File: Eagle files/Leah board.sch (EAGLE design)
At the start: 2 parts

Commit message: Board Tweaks
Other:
- note removed: "Adafruit Pro Trinket 5V"
- note removed: "CC 2.5 BY-SA"
- note removed: "http://adafruit.com/products/2000"
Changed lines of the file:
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@@
 <sheet>
 <plain>
-<text x="175.26" y="30.48" size="2.54" layer="94">Adafruit Pro Trinket 5V</text>
-<text x="175.26" y="25.4" size="2.54" layer="94">http://adafruit.com/products/2000</text>
-<text x="248.92" y="30.48" size="2.54" layer="94">CC 2.5 BY-SA</text>
 </plain>
 <instances>

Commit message: Board work
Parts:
- added CONT_LED, INT_LED, LASER, POWER, PWR_LED: (no value), adafruit:JST_2PIN-SMT-RA
- added POT: (no value), adafruit:JST_3PIN
- added X_SERVO, Y_SERVO: (no value), adafruit:PINHD-1X3
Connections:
- removed net VBAT: JP1.1
- new net VCC: JP1.1, POWER.2
- net A2: now also POT.2
- net GND: now also LASER.1, POWER.1

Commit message: Modification for present.
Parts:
- added CONT_MOS, INT_MOS, LASER_MOS, PWR_MOS, X_MOS, Y_MOS: 200mA/50V, SparkFun-DiscreteSemi:MOSFET-NCHANNELBSS138
- added R1, R2, R3, R4, R5, R6: 10K, SparkFun-Resistors:10KOHM-1/10W-1%(0603)0603
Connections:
- new net CONT_PWR: CONT_LED.2, CONT_MOS.S, R2.2
- new net INT_PWR: INT_LED.2, INT_MOS.S, R1.2
- new net LASER_PIN: LASER_MOS.G
- new net N$2: INT_MOS.G
- new net N$3: CONT_MOS.G
- new net N$4: PWR_MOS.G
- new net N$5: LASER_MOS.S, R4.2
- new net N$6: R6.2, Y_MOS.S, Y_SERVO.2
- new net N$7: R5.2, X_MOS.S, X_SERVO.2
- new net PLED_PWR: PWR_LED.2, PWR_MOS.S, R3.2
- new net XSERVO_PWR_PIN: X_MOS.G
- new net YSERVO_PWR_PIN: Y_MOS.G
- net A0: now also X_SERVO.3
- net A1: now also Y_SERVO.1
- net GND: now also CONT_LED.1, INT_LED.1, POT.3, PWR_LED.1, R1.1, R2.1, R3.1, R4.1, R5.1, R6.1, X_SERVO.1, Y_SERVO.3
- net VCC: now also CONT_MOS.D, INT_MOS.D, LASER_MOS.D, POT.1, PWR_MOS.D, X_MOS.D, Y_MOS.D
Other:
- note added: "LEDs"
- note added: "Servo Control"
- moved on the sheet: CONT_LED, INT_LED, LASER, PWR_LED, X_SERVO, Y_SERVO

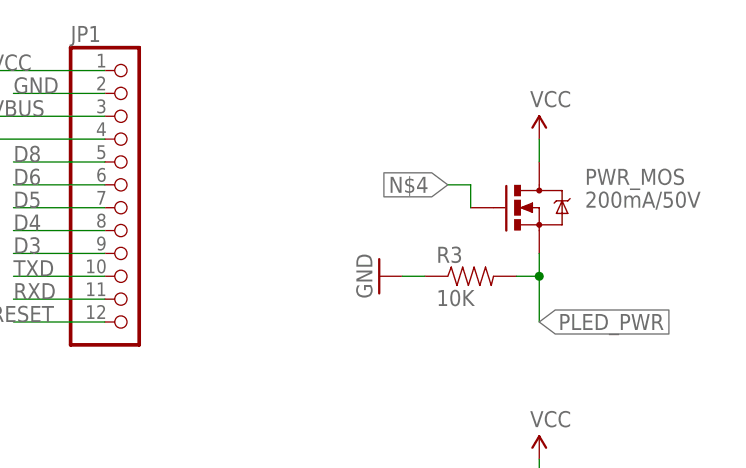
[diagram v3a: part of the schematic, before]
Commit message: Added base Event class and timer class
Timer and Task classes are now derived from Event class
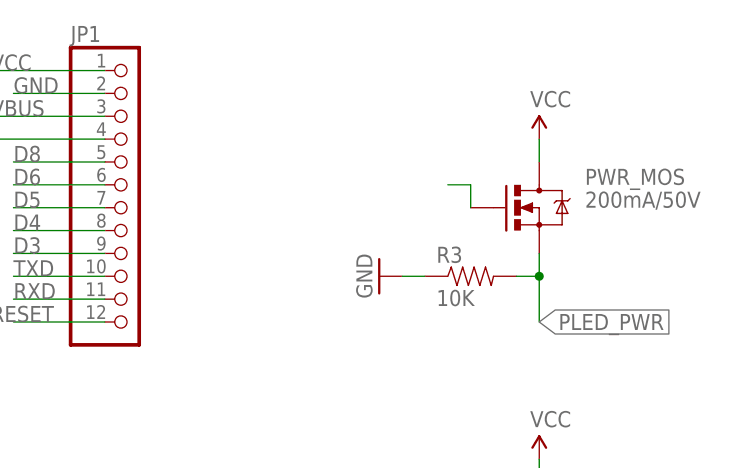
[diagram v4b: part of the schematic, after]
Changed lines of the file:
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@@
 <wire x1="213.36" y1="177.8" x2="213.36" y2="180.34" width="0.1524" layer="91"/>
 <wire x1="213.36" y1="180.34" x2="210.82" y2="180.34" width="0.1524" layer="91"/>
-<label x="210.82" y="180.34" size="1.778" layer="95" rot="R180" xref="yes"/>
 </segment>
 </net>

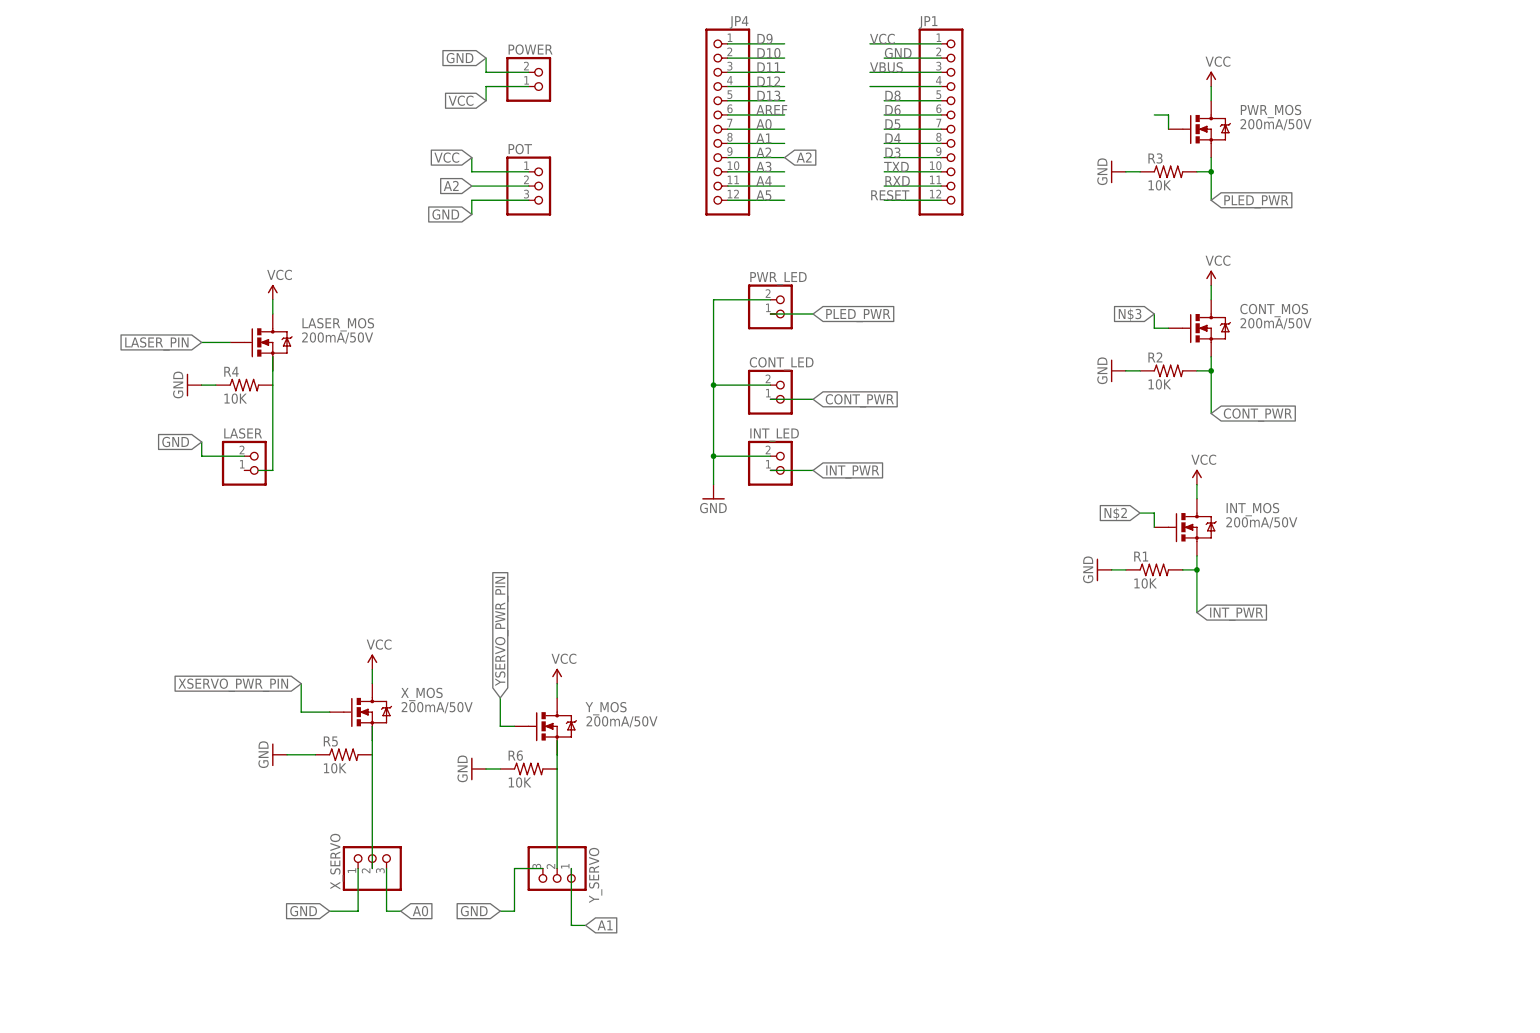
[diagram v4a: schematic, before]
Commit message: Routed board
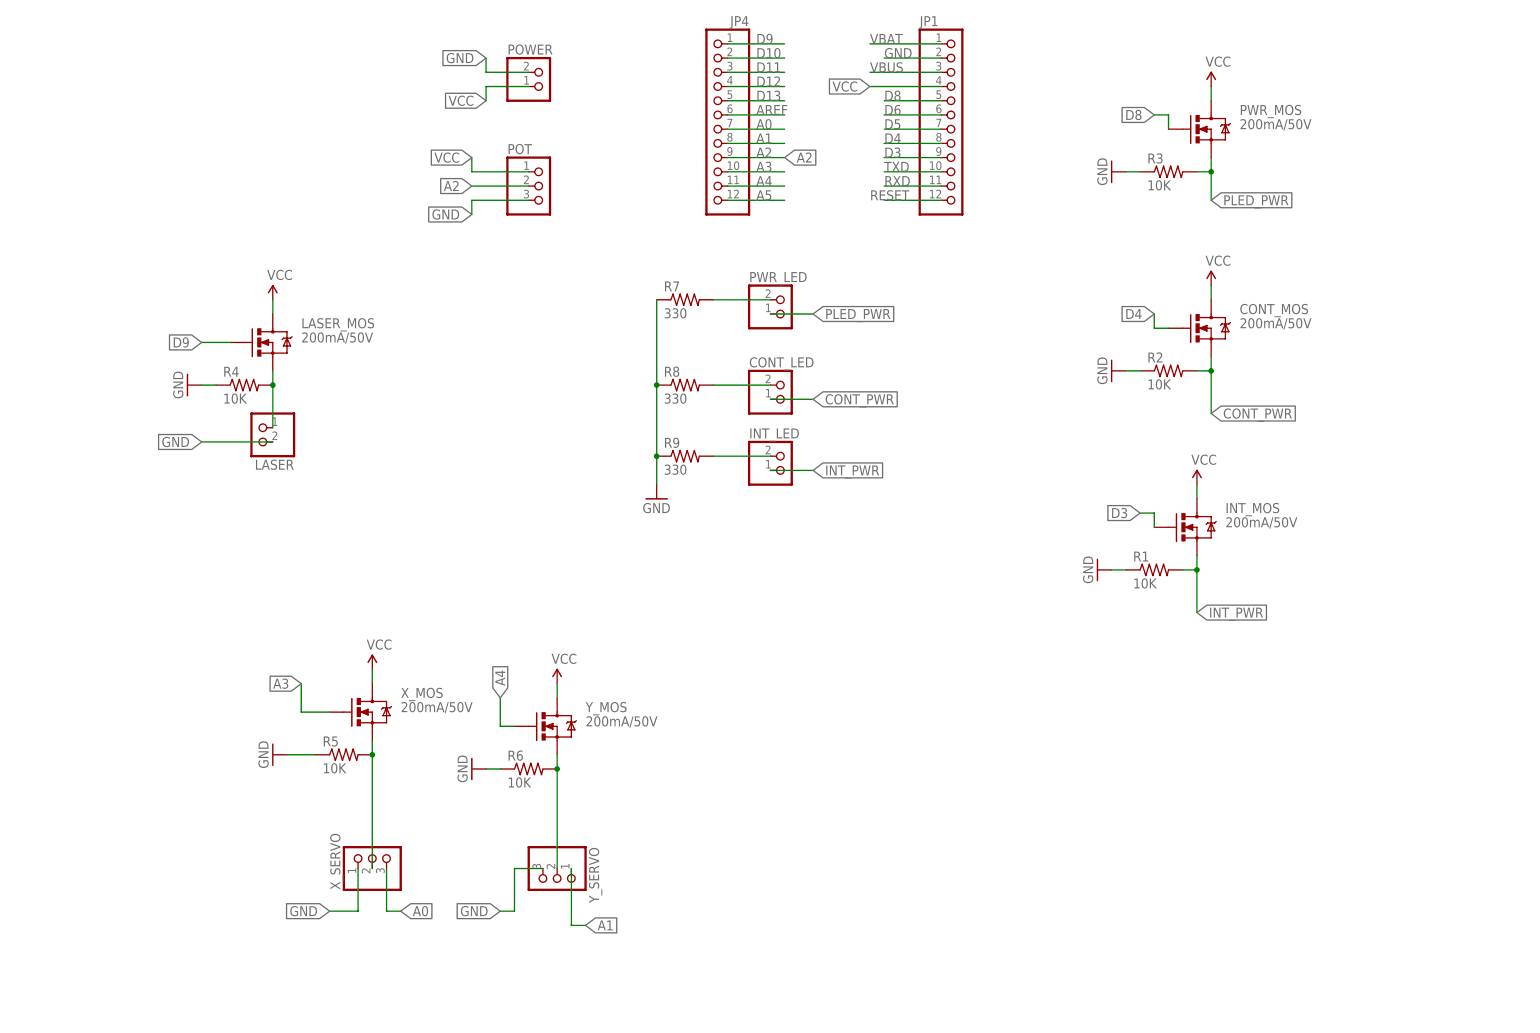
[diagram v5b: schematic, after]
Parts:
- added R7, R8, R9: 330, SparkFun-Resistors:3.3MOHM-1/10W-1%(0603)
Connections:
- removed net LASER_PIN: LASER_MOS.G
- removed net N$1: JP1.4
- removed net N$2: INT_MOS.G
- removed net N$3: CONT_MOS.G
- removed net N$4: PWR_MOS.G
- removed net N$5: LASER_MOS.S, R4.2
- removed net XSERVO_PWR_PIN: X_MOS.G
- removed net YSERVO_PWR_PIN: Y_MOS.G
- new net LASER_PWR: LASER.2, LASER_MOS.S, R4.2
- new net N$10: INT_LED.1, R9.2
- new net N$8: PWR_LED.1, R7.2
- new net N$9: CONT_LED.1, R8.2
- new net VBAT: JP1.1
- net A3: now also X_MOS.G
- net A4: now also Y_MOS.G
- net D3: now also INT_MOS.G
- net D4: now also CONT_MOS.G
- net D8: now also PWR_MOS.G
- net D9: now also LASER_MOS.G
- net GND: now also R7.1, R8.1, R9.1; no longer CONT_LED.1, INT_LED.1, PWR_LED.1
- net VCC: now also JP1.4; no longer JP1.1
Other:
- moved on the sheet: LASER

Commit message: Tweaks
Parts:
- removed CONT_LED, PWR_LED: (no value), adafruit:JST_2PIN-SMT-RA
- removed CONT_MOS: 200mA/50V, SparkFun-DiscreteSemi:MOSFET-NCHANNELBSS138
- added C1: 100uF, SparkFun-Capacitors:100UF-10V-10%(TANT)
- added R10: 39, SparkFun-Resistors:10KOHM-1/10W-1%(0603)0603
- added RUN_LED, SLP_LED: (no value), adafruit:JST_2PIN-SMT-RA
- added SLEEP_MOS: 200mA/50V, SparkFun-DiscreteSemi:MOSFET-NCHANNELBSS138
- X_MOS, Y_MOS: value 200mA/50V -> 2.6A/20V
- renumbered PWR_MOS to RUN_MOS
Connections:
- net A0 renamed X_PWM_PIN
- net A1 renamed Y_PWM_PIN
- net A2 renamed POT_IN
- net A3 renamed X_PWR_PIN
- net A4 renamed Y_PWR_PIN
- net D8 renamed RUN_LED_PIN
- net D9 renamed LASER_PIN
- removed net CONT_PWR: CONT_LED.2, CONT_MOS.S, R2.2
- removed net D3: INT_MOS.G, JP1.9
- removed net D4: CONT_MOS.G, JP1.8
- removed net INT_PWR: INT_LED.2, INT_MOS.S, R1.2
- removed net PLED_PWR: PWR_LED.2, R3.2, RUN_MOS.S
- removed net VCC: CONT_MOS.D, INT_MOS.D, JP1.4, LASER_MOS.D, POT.1, POWER.2, RUN_MOS.D, X_MOS.D, Y_MOS.D
- new net 5V: JP1.4, POT.1
- new net INT_LED_PIN: INT_MOS.G, JP1.8
- new net INT_LED_PWR: INT_LED.2, INT_MOS.S, R2.2
- new net N$1: C1.+, LASER.2, R10.1
- new net RUN_LED_PWR: R3.2, RUN_LED.2, RUN_MOS.S
- new net SLP_LED_PIN: JP1.9, SLEEP_MOS.G
- new net SLP_LED_PWR: R1.2, SLEEP_MOS.S, SLP_LED.2
- net GND: now also C1.-
- net LASER_PWR: now also R10.2; no longer LASER.2
- net N$10: now also SLP_LED.1; no longer INT_LED.1
- net N$8: now also RUN_LED.1; no longer PWR_LED.1
- net N$9: now also INT_LED.1; no longer CONT_LED.1
- net VBAT: now also INT_MOS.D, LASER_MOS.D, POWER.2, RUN_MOS.D, SLEEP_MOS.D, X_MOS.D, Y_MOS.D
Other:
- note added: "-> LEDS"
- note added: "->LASER DIODE"
- note added: "10K Potentiometer ->"
- note added: "LED JST Connectors"
- note added: "LED Power Control"
- note added: "Low Pass Filter"
- note added: "Max Servo Power Draw: 200mA each Avg Servo Power Draw: 90mA each"
- note added: "Pro Trinket Interface"
- note added: "Servo Position Control"
- note added: "Servo Power Control"
- note removed: "LEDs"
- note removed: "Servo Control"
- moved on the sheet: INT_LED, INT_MOS, JP1, JP4, LASER, LASER_MOS, R4, R7, R8, R9
